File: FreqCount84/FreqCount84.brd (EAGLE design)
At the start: 160 x 100 mm, 46 parts, among them IC1 74LS595D, IC2 74LS595D, IC3 74LS595D, IC4 74S151D, IC5 7805T, Q1 20.000MHz

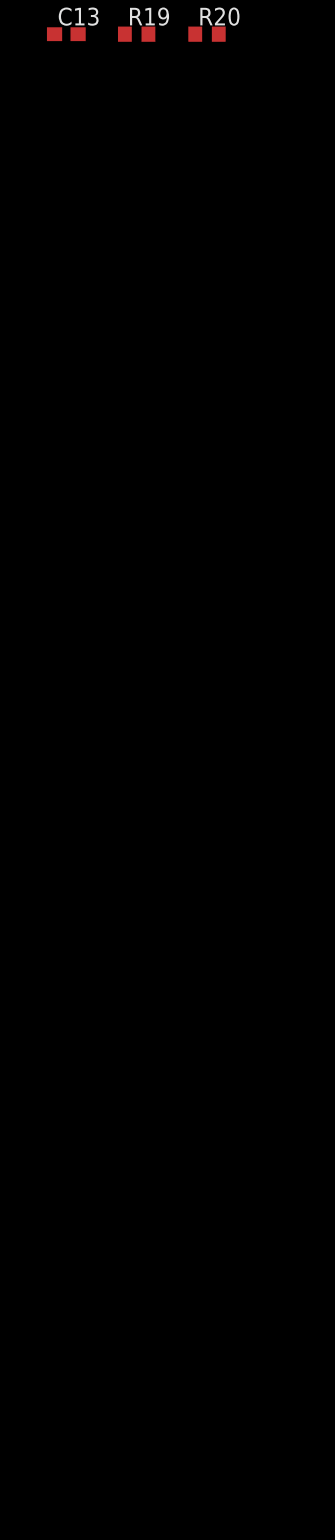
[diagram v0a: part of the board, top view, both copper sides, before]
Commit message: FreqCount84 adding Input Stage (AC / DC coupling and Amplification); updated resistor and capacitor libraries so that the values and names are on the same side of the symbol rather than opposite sides
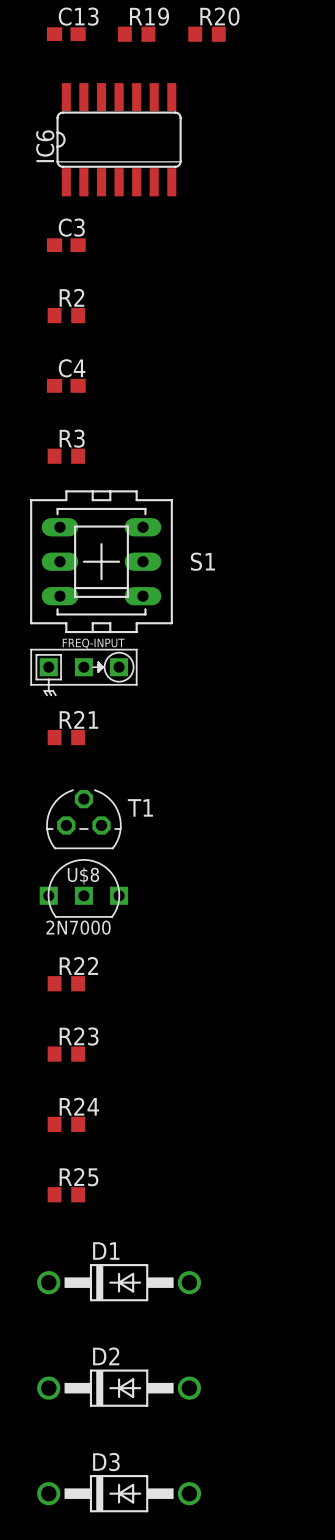
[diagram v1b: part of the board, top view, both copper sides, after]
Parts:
- added C3, C4: 0.1u, rcl:C0603
- added D1, D2, D3: 1N4004, diode:DO41-10
- added FREQ-INPUT: I/O, !synth_sch:MONO_JACK
- added IC6: 74AHCU04, 74xx-us:SO14
- added R2: 1, rcl:R0603
- added R21, R24: 1M, rcl:R0603
- added R22, R23: 1k, rcl:R0603
- added R25: 10k, rcl:R0603
- added R3: 100k, rcl:R0603
- added S1: PVA2R, switch-misc:PVA2R
- added T1: 2N3904, transistor:TO92
- added U$8: 2N7000, !synth_sch:2N7000
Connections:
- removed net FREQ-IN: IC4.4, V1.10
- new net FREQ-AC-COUPLED: IC6.12, S1.6
- new net FREQ-DC-COUPLED: R23.2, R24.1, S1.4, U$8.D
- new net FREQ-DIGITAL-IN: IC4.4, S1.5, V1.10
- new net N$22: IC6.2, IC6.3, R3.2
- new net N$23: IC6.6, IC6.9
- new net N$42: IC6.11, IC6.8
- new net N$43: IC6.10, IC6.13
- new net N$44: IC6.4, IC6.5
- new net N$45: C3.1, IC6.14, R2.1
- new net N$46: R22.2, T1.1, U$8.G
- new net N$47: C4.1, S1.3
- new net N$49: R25.2, S1.1
- new net N$50: FREQ-INPUT.P$2, S1.2
- new net N$52: C4.2, D2.C, D3.A, IC6.1, R21.1, R3.1
- new net N$54: D1.C, R24.2, R25.1, T1.2
- net +5V: now also D3.C, R2.2, R22.1, R23.1
- net GND: now also C3.2, D1.A, D2.A, FREQ-INPUT.P$1, FREQ-INPUT.P$3, IC6.7, R21.2, T1.3, U$8.S
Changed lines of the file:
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@@
 <element name="C13" library="rcl" package="C0603" value="0.1u" x="-81.28" y="-195.58"/>
 <element name="R20" library="rcl" package="R0603" value="1" x="-71.12" y="-195.58"/>
+<element name="IC6" library="74xx-us" package="SO14" value="74AHCU04" x="-77.47" y="-203.2"/>
+<element name="C3" library="rcl" package="C0603" value="0.1u" x="-81.28" y="-210.82"/>
+<element name="R2" library="rcl" package="R0603" value="1" x="-81.28" y="-215.9"/>
+<element name="C4" library="rcl" package="C0603" value="0.1u" x="-81.28" y="-220.98"/>
+<element name="R3" library="rcl" package="R0603" value="100k" x="-81.28" y="-226.06"/>
+<element name="S1" library="switch-misc" package="PVA2R" value="PVA2R" x="-78.74" y="-233.68"/>
+<element name="FREQ-INPUT" library="!synth_sch" package="MONO_JACK" value="I/O" x="-80.01" y="-241.3"/>
+<element name="R21" library="rcl" package="R0603" value="1M" x="-81.28" y="-246.38"/>
+<element name="T1" library="transistor" package="TO92" value="2N3904" x="-80.01" y="-252.73"/>
+<element name="U$8" library="!synth_sch" package="2N7000" value="2N7000" x="-80.01" y="-257.81"/>
+<element name="R22" library="rcl" package="R0603" value="1k" x="-81.28" y="-264.16"/>
+<element name="R23" library="rcl" package="R0603" value="1k" x="-81.28" y="-269.24"/>
+<element name="R24" library="rcl" package="R0603" value="1M" x="-81.28" y="-274.32"/>
+<element name="R25" library="rcl" package="R0603" value="10k" x="-81.28" y="-279.4"/>
+<element name="D1" library="diode" package="DO41-10" value="1N4004" x="-77.47" y="-285.75"/>
+<element name="D2" library="diode" package="DO41-10" value="1N4004" x="-77.47" y="-293.37"/>
+<element name="D3" library="diode" package="DO41-10" value="1N4004" x="-77.47" y="-300.99"/>
 </elements>
 <signals>
@@
 <contactref element="C13" pad="2"/>
 <contactref element="V1" pad="16"/>
+<contactref element="IC6" pad="7"/>
+<contactref element="C3" pad="2"/>
+<contactref element="R21" pad="2"/>
+<contactref element="U$8" pad="S"/>
+<contactref element="T1" pad="3"/>
+<contactref element="FREQ-INPUT" pad="P$3"/>
+<contactref element="FREQ-INPUT" pad="P$1"/>
+<contactref element="D1" pad="A"/>
+<contactref element="D2" pad="A"/>
 <wire x1="-71.755" y1="-191.0334" x2="-67.73" y2="-186.69" width="0" layer="19" extent="1-1"/>
 <wire x1="-73.025" y1="-191.0334" x2="-71.755" y2="-191.0334" width="0" layer="19" extent="1-1"/>
@@
 <wire x1="-80.01" y1="-173.99" x2="-75.565" y2="-184.8866" width="0" layer="19" extent="1-1"/>
 <wire x1="-82.13" y1="-168.91" x2="-80.01" y2="-173.99" width="0" layer="19" extent="1-1"/>
+<wire x1="-73.66" y1="-206.2734" x2="-80.43" y2="-195.58" width="0" layer="19" extent="1-1"/>
+<wire x1="-80.43" y1="-210.82" x2="-73.66" y2="-206.2734" width="0" layer="19" extent="1-1"/>
 <wire x1="-67.31" y1="-173.99" x2="-67.73" y2="-186.69" width="0" layer="19" extent="1-1"/>
+<wire x1="-80.01" y1="-241.3" x2="-80.43" y2="-210.82" width="0" layer="19" extent="1-1"/>
+<wire x1="-82.55" y1="-241.3" x2="-80.01" y2="-241.3" width="0" layer="19" extent="1-1"/>
+<wire x1="-80.43" y1="-246.38" x2="-80.01" y2="-241.3" width="0" layer="19" extent="1-1"/>
+<wire x1="-81.28" y1="-252.73" x2="-80.43" y2="-246.38" width="0" layer="19" extent="1-1"/>
+<wire x1="-82.55" y1="-257.81" x2="-81.28" y2="-252.73" width="0" layer="19" extent="1-1"/>
+<wire x1="-72.39" y1="-285.75" x2="-82.55" y2="-257.81" width="0" layer="19" extent="1-1"/>
+<wire x1="-72.39" y1="-293.37" x2="-72.39" y2="-285.75" width="0" layer="19" extent="1-1"/>
 <wire x1="-82.55" y1="-101.6" x2="-82.13" y2="-168.91" width="0" layer="19" extent="1-1"/>
 <wire x1="-82.55" y1="-95.25" x2="-82.55" y2="-101.6" width="0" layer="19" extent="1-1"/>
@@
 <contactref element="R19" pad="2"/>
 <contactref element="R20" pad="2"/>
+<contactref element="R2" pad="2"/>
+<contactref element="R23" pad="1"/>
+<contactref element="R22" pad="1"/>
+<contactref element="D3" pad="C"/>
+<wire x1="-82.13" y1="-269.24" x2="-82.55" y2="-300.99" width="0" layer="19" extent="1-1"/>
+<wire x1="-82.13" y1="-264.16" x2="-82.13" y2="-269.24" width="0" layer="19" extent="1-1"/>
+<wire x1="-80.43" y1="-215.9" x2="-82.13" y2="-264.16" width="0" layer="19" extent="1-1"/>
+<wire x1="-75.35" y1="-195.58" x2="-80.43" y2="-215.9" width="0" layer="19" extent="1-1"/>
+<wire x1="-70.27" y1="-195.58" x2="-75.35" y2="-195.58" width="0" layer="19" extent="1-1"/>
+<wire x1="-80.43" y1="-40.64" x2="-75.35" y2="-195.58" width="0" layer="19" extent="1-1"/>
 <wire x1="-80.43" y1="-35.56" x2="-80.43" y2="-40.64" width="0" layer="19" extent="1-1"/>
 <wire x1="-73.025" y1="-19.7866" x2="-80.43" y2="-35.56" width="0" layer="19" extent="1-1"/>
@@
 <wire x1="-19.05" y1="2.54" x2="-43.815" y2="-21.0566" width="0" layer="19" extent="1-1"/>
 <wire x1="-31.75" y1="50.8" x2="-65.19" y2="20.32" width="0" layer="19" extent="1-1"/>
-<wire x1="-75.35" y1="-195.58" x2="-80.43" y2="-40.64" width="0" layer="19" extent="1-1"/>
-<wire x1="-70.27" y1="-195.58" x2="-75.35" y2="-195.58" width="0" layer="19" extent="1-1"/>
 </signal>
 <signal name="SR_DATA">
@@
 <wire x1="-71.755" y1="-184.8866" x2="-74.295" y2="-17.0434" width="0" layer="19" extent="1-1"/>
 </signal>
-<signal name="FREQ-IN">
+<signal name="FREQ-DIGITAL-IN">
 <contactref element="IC4" pad="4"/>
 <contactref element="V1" pad="10"/>
+<contactref element="S1" pad="5"/>
 <wire x1="-76.835" y1="-191.0334" x2="-64.77" y2="-173.99" width="0" layer="19" extent="1-1"/>
+<wire x1="-75.7428" y1="-233.68" x2="-76.835" y2="-191.0334" width="0" layer="19" extent="1-1"/>
 </signal>
 <signal name="N$38">
@@
 <wire x1="-80.645" y1="-184.8866" x2="-82.13" y2="-195.58" width="0" layer="19" extent="1-1"/>
 </signal>
+<signal name="N$22">
+<contactref element="IC6" pad="2"/>
+<contactref element="IC6" pad="3"/>
+<contactref element="R3" pad="2"/>
+<wire x1="-80.01" y1="-206.2734" x2="-80.43" y2="-226.06" width="0" layer="19" extent="1-1"/>
+<wire x1="-78.74" y1="-206.2734" x2="-80.01" y2="-206.2734" width="0" layer="19" extent="1-1"/>
+</signal>
+<signal name="N$23">
+<contactref element="IC6" pad="6"/>
+<contactref element="IC6" pad="9"/>
+<wire x1="-74.93" y1="-200.1266" x2="-74.93" y2="-206.2734" width="0" layer="19" extent="1-1"/>
+</signal>
+<signal name="N$42">
+<contactref element="IC6" pad="8"/>
+<contactref element="IC6" pad="11"/>
+<wire x1="-73.66" y1="-200.1266" x2="-77.47" y2="-200.1266" width="0" layer="19" extent="1-1"/>
+</signal>
+<signal name="N$43">
+<contactref element="IC6" pad="10"/>
+<contactref element="IC6" pad="13"/>
+<wire x1="-76.2" y1="-200.1266" x2="-80.01" y2="-200.1266" width="0" layer="19" extent="1-1"/>
+</signal>
+<signal name="N$44">
+<contactref element="IC6" pad="4"/>
+<contactref element="IC6" pad="5"/>
+<wire x1="-76.2" y1="-206.2734" x2="-77.47" y2="-206.2734" width="0" layer="19" extent="1-1"/>
+</signal>
+<signal name="N$45">
+<contactref element="R2" pad="1"/>
+<contactref element="C3" pad="1"/>
+<contactref element="IC6" pad="14"/>
+<wire x1="-82.13" y1="-210.82" x2="-82.13" y2="-215.9" width="0" layer="19" extent="1-1"/>
+<wire x1="-81.28" y1="-200.1266" x2="-82.13" y2="-210.82" width="0" layer="19" extent="1-1"/>
+</signal>
+<signal name="N$47">
+<contactref element="C4" pad="1"/>
+<contactref element="S1" pad="3"/>
+<wire x1="-82.13" y1="-220.98" x2="-81.7372" y2="-236.1692" width="0" layer="19" extent="1-1"/>
+</signal>
+<signal name="N$50">
+<contactref element="FREQ-INPUT" pad="P$2"/>
+<contactref element="S1" pad="2"/>
+<wire x1="-81.7372" y1="-233.68" x2="-77.47" y2="-241.3" width="0" layer="19" extent="1-1"/>
+</signal>
+<signal name="N$52">
+<contactref element="C4" pad="2"/>
+<contactref element="IC6" pad="1"/>
+<contactref element="R21" pad="1"/>
+<contactref element="D2" pad="C"/>
+<contactref element="D3" pad="A"/>
+<contactref element="R3" pad="1"/>
+<wire x1="-72.39" y1="-300.99" x2="-82.55" y2="-293.37" width="0" layer="19" extent="1-1"/>
+<wire x1="-82.13" y1="-246.38" x2="-82.55" y2="-293.37" width="0" layer="19" extent="1-1"/>
+<wire x1="-82.13" y1="-226.06" x2="-82.13" y2="-246.38" width="0" layer="19" extent="1-1"/>
+<wire x1="-80.43" y1="-220.98" x2="-82.13" y2="-226.06" width="0" layer="19" extent="1-1"/>
+<wire x1="-81.28" y1="-206.2734" x2="-80.43" y2="-220.98" width="0" layer="19" extent="1-1"/>
+</signal>
+<signal name="N$46">
+<contactref element="U$8" pad="G"/>
+<contactref element="R22" pad="2"/>
+<contactref element="T1" pad="1"/>
+<wire x1="-80.01" y1="-257.81" x2="-80.43" y2="-264.16" width="0" layer="19" extent="1-1"/>
+<wire x1="-78.74" y1="-252.73" x2="-80.01" y2="-257.81" width="0" layer="19" extent="1-1"/>
+</signal>
+<signal name="FREQ-DC-COUPLED">
+<contactref element="R23" pad="2"/>
+<contactref element="U$8" pad="D"/>
+<contactref element="R24" pad="1"/>
+<contactref element="S1" pad="4"/>
+<wire x1="-80.43" y1="-269.24" x2="-82.13" y2="-274.32" width="0" layer="19" extent="1-1"/>
+<wire x1="-77.47" y1="-257.81" x2="-80.43" y2="-269.24" width="0" layer="19" extent="1-1"/>
+<wire x1="-75.7428" y1="-231.1908" x2="-77.47" y2="-257.81" width="0" layer="19" extent="1-1"/>
+</signal>
+<signal name="N$54">
+<contactref element="T1" pad="2"/>
+<contactref element="R24" pad="2"/>
+<contactref element="R25" pad="1"/>
+<contactref element="D1" pad="C"/>
+<wire x1="-82.13" y1="-279.4" x2="-82.55" y2="-285.75" width="0" layer="19" extent="1-1"/>
+<wire x1="-80.43" y1="-274.32" x2="-82.13" y2="-279.4" width="0" layer="19" extent="1-1"/>
+<wire x1="-80.01" y1="-250.825" x2="-80.43" y2="-274.32" width="0" layer="19" extent="1-1"/>
+</signal>
+<signal name="FREQ-AC-COUPLED">
+<contactref element="S1" pad="6"/>
+<contactref element="IC6" pad="12"/>
+<wire x1="-78.74" y1="-200.1266" x2="-75.7428" y2="-236.1692" width="0" layer="19" extent="1-1"/>
+</signal>
+<signal name="N$49">
+<contactref element="S1" pad="1"/>
+<contactref element="R25" pad="2"/>
+<wire x1="-81.7372" y1="-231.1908" x2="-80.43" y2="-279.4" width="0" layer="19" extent="1-1"/>
+</signal>
 </signals>
